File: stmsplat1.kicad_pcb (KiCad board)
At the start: 2 copper layers, 14 parts, among them CN1 C_Pack04, CN10 Conn_01x34_Male, CN7 Conn_01x20_Male, CN8 Conn_01x16_Male, CN9 Conn_01x30_Male, J1 Conn_Coaxial, J2 Conn_Coaxial, J3 Conn_Coaxial, U1 NUCLEO144-F746ZG, U2 SA630D-RF_Switch, U3 MCP6S93-X_UN, U4 ublox_chinese_PCB_module

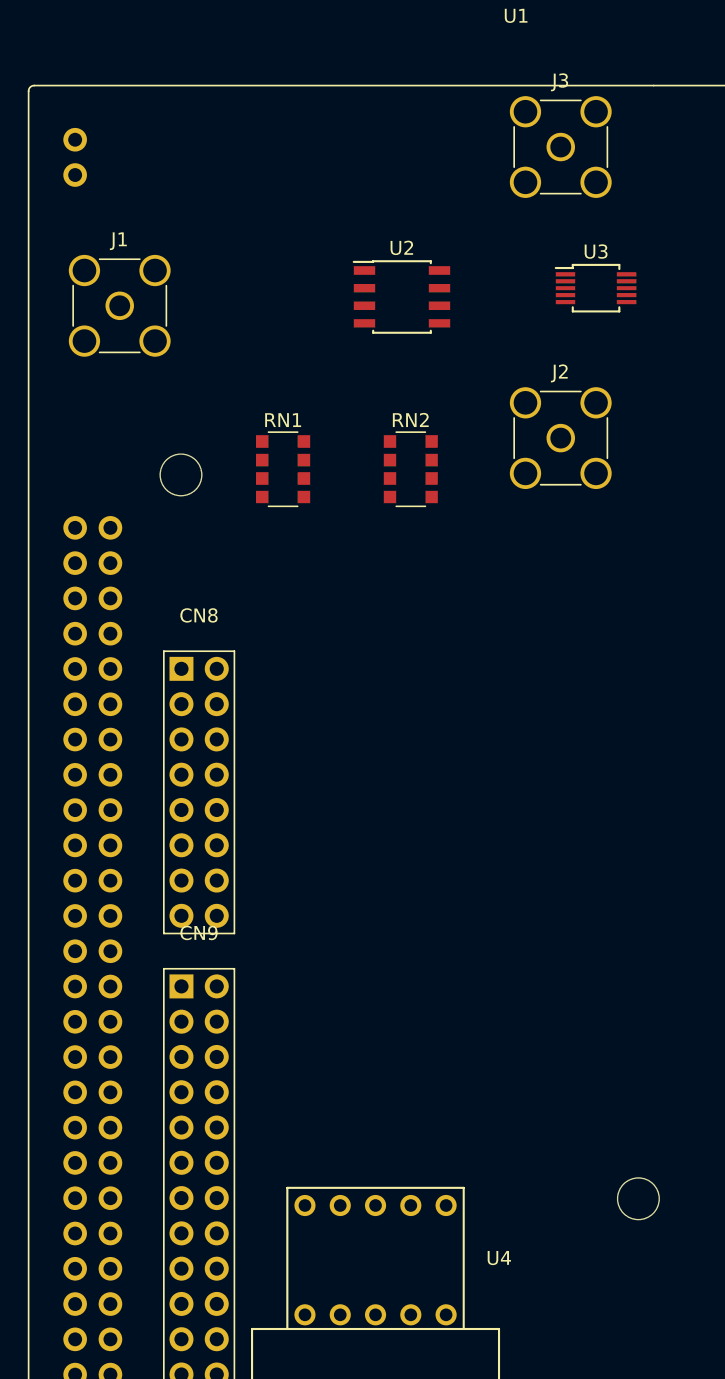
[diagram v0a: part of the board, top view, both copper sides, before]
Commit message: Added input lowpass filter
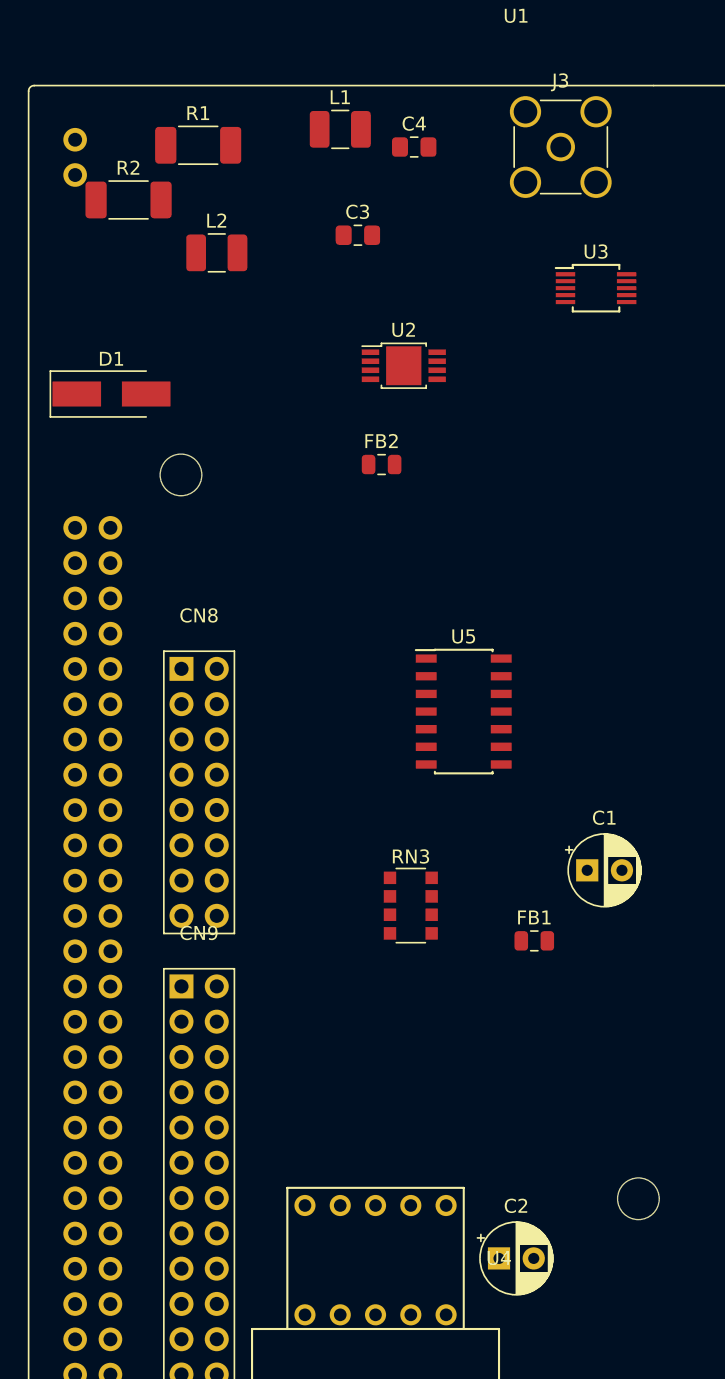
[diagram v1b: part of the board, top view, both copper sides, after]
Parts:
- removed J1, J2: Conn_Coaxial, Connector_Coaxial:SMA_Amphenol_132134-11_Vertical
- removed RN1, RN2: R_Pack04, Resistor_SMD:R_Array_Convex_4x1206
- added C1: 1uF, Capacitor_THT:CP_Radial_D5.0mm_P2.50mm, F.Cu at (95.2, 90.2)
- added C2: 1uF, Capacitor_THT:CP_Radial_D5.0mm_P2.50mm, F.Cu at (88.9, 118.1)
- added C3: 560pF, Capacitor_SMD:C_0805_2012Metric_Pad1.15x1.40mm_HandSolder, F.Cu at (78.7, 44.5)
- added C4: 240pF, Capacitor_SMD:C_0805_2012Metric_Pad1.15x1.40mm_HandSolder, F.Cu at (82.8, 38.1)
- added D1: SMAJ8.0CA Bourns 9V, Diode_SMD:D_SMA_Handsoldering, F.Cu at (61.0, 55.9)
- added FB1: Ferrite_Bead, Inductor_SMD:L_0805_2012Metric, F.Cu at (91.4, 95.2)
- added FB2: Ferrite_Bead, Inductor_SMD:L_0805_2012Metric, F.Cu at (80.4, 61.0)
- added L1: 620nH, Inductor_SMD:L_1210_3225Metric_Pad1.42x2.65mm_HandSolder, F.Cu at (77.5, 36.8)
- added L2: 1.5uH, Inductor_SMD:L_1210_3225Metric_Pad1.42x2.65mm_HandSolder, F.Cu at (68.6, 45.7)
- added R1: 100R, Resistor_SMD:R_2010_5025Metric_Pad1.52x2.65mm_HandSolder, F.Cu at (67.2, 38.0)
- added R2: 100R, Resistor_SMD:R_2010_5025Metric_Pad1.52x2.65mm_HandSolder, F.Cu at (62.2, 41.9)
- added RN3: 4K7, Resistor_SMD:R_Array_Convex_4x1206, F.Cu at (82.5, 92.7)
- added U5: Opamp_Quad_MCP6024, Package_SO:SOIC-14_3.9x8.7mm_P1.27mm, F.Cu at (86.4, 78.7)
- CN1: value C_Pack04 -> 10n
- U2: value SA630D-RF_Switch -> AD8310; footprint Package_SO:SOIC-8_3.9x4.9mm_P1.27mm -> Package_SO:MSOP-8-1EP_3x3mm_P0.65mm_EP2.54x2.8mm
- moved U2 4.95 mm to (82.0, 53.8)
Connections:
- CN10 pad 17: /GND -> GND
- CN10 pad 22: /GND -> GND
- CN10 pad 27: /GND -> GND
- CN10 pad 5: /GND -> GND
- CN7 pad 8: /GND -> GND
- CN8 pad 11: /GND -> GND
- CN9 pad 12: /GND -> GND
- CN9 pad 23: /GND -> GND
- J3 pad 1: Net-(J3-Pad1) -> Net-(D1-Pad1)
- J3 pad 2: Net-(J3-Pad2) -> /AGND
- U2 pad 2: Net-(U2-Pad2) -> /AGND
- U2 pad 5: Net-(J2-Pad1) -> /A3V3
- U2 pad 8: Net-(J3-Pad1) -> Net-(U2-Pad8)
- U3 pad 3: Net-(U3-Pad3) -> Net-(U2-Pad4)
- U3 pad 5: Net-(U3-Pad5) -> /AGND
- U4 pad 1: Net-(U4-Pad1) -> /+3V3
- U4 pad 2: Net-(U4-Pad2) -> GND

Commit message: Added more
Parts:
- added C10: 47n, Capacitor_SMD:C_1210_3225Metric_Pad1.42x2.65mm_HandSolder, F.Cu at (36.8, 92.4)
- added C11: 47n, Capacitor_SMD:C_1210_3225Metric_Pad1.42x2.65mm_HandSolder, F.Cu at (41.7, 89.2)
- added C12: 1uF, Capacitor_THT:CP_Radial_D5.0mm_P2.50mm, F.Cu at (33.9, 109.5)
- added C13: 10uF, Capacitor_THT:CP_Radial_D5.0mm_P2.50mm, F.Cu at (39.5, 109.5)
- added C14: 1uF, Capacitor_THT:CP_Radial_D5.0mm_P2.50mm, F.Cu at (28.3, 109.5)
- added C15: 100nF, Capacitor_THT:C_Disc_D7.5mm_W2.5mm_P5.00mm, F.Cu at (38.4, 30.7)
- added C16: 100uF, Capacitor_THT:CP_Radial_D5.0mm_P2.50mm, F.Cu at (46.5, 32.0)
- added C17: 100uF, Capacitor_THT:CP_Radial_D5.0mm_P2.50mm, F.Cu at (38.4, 35.0)
- added C5: 47n, Capacitor_SMD:C_1210_3225Metric_Pad1.42x2.65mm_HandSolder, F.Cu at (36.6, 64.5)
- added C6: 47n, Capacitor_SMD:C_1210_3225Metric_Pad1.42x2.65mm_HandSolder, F.Cu at (41.5, 61.3)
- added C7: 47n, Capacitor_SMD:C_1210_3225Metric_Pad1.42x2.65mm_HandSolder, F.Cu at (36.6, 61.3)
- added C8: 25pF, Capacitor_THT:C_Disc_D7.5mm_W2.5mm_P5.00mm, F.Cu at (22.9, 82.5)
- added C9: 47n, Capacitor_SMD:C_1210_3225Metric_Pad1.42x2.65mm_HandSolder, F.Cu at (36.8, 89.2)
- added D2: LED, LED_SMD:LED_PLCC-2, F.Cu at (35.1, 145.1)
- added D3: LED, LED_SMD:LED_PLCC-2, F.Cu at (35.5, 141.6)
- added D4: LED, LED_SMD:LED_PLCC-2, F.Cu at (40.7, 141.6)
- added D5: LED, LED_SMD:LED_PLCC-2, F.Cu at (39.6, 133.4)
- added D6: LED, LED_SMD:LED_PLCC-2, F.Cu at (45.0, 118.1)
- added D7: LED, LED_SMD:LED_PLCC-2, F.Cu at (34.4, 133.4)
- added J2: Conn_01x04_Male, Connector_PinHeader_2.54mm:PinHeader_1x04_P2.54mm_Vertical, F.Cu at (28.5, 36.1)
- added R3: 53R, Capacitor_SMD:C_1210_3225Metric_Pad1.42x2.65mm_HandSolder, F.Cu at (29.1, 70.6)
- added RN2: 470R, Resistor_SMD:R_Array_Convex_4x1206, F.Cu at (38.4, 123.5)
- added RN3: 470R, Resistor_SMD:R_Array_Convex_4x1206, F.Cu at (34.0, 123.5)
- added TP10: TestPoint, TestPoint:TestPoint_Loop_D1.80mm_Drill1.0mm_Beaded, F.Cu at (45.6, 68.8)
- added TP11: TestPoint, TestPoint:TestPoint_Loop_D1.80mm_Drill1.0mm_Beaded, F.Cu at (41.9, 72.5)
- added TP12: TestPoint, TestPoint:TestPoint_Loop_D1.80mm_Drill1.0mm_Beaded, F.Cu at (45.8, 61.5)
- added TP13: TestPoint, TestPoint:TestPoint_Loop_D1.80mm_Drill1.0mm_Beaded, F.Cu at (49.2, 68.8)
- added TP3: TestPoint, TestPoint:TestPoint_Loop_D1.80mm_Drill1.0mm_Beaded, F.Cu at (44.5, 65.2)
- added TP4: TestPoint, TestPoint:TestPoint_Loop_D1.80mm_Drill1.0mm_Beaded, F.Cu at (38.3, 72.0)
- added TP5: TestPoint, TestPoint:TestPoint_Loop_D1.80mm_Drill1.0mm_Beaded, F.Cu at (49.5, 61.5)
- added TP6: TestPoint, TestPoint:TestPoint_Loop_D1.80mm_Drill1.0mm_Beaded, F.Cu at (69.8, 68.6)
- added TP7: TestPoint, TestPoint:TestPoint_Loop_D1.80mm_Drill1.0mm_Beaded, F.Cu at (41.9, 68.8)
- added TP8: TestPoint, TestPoint:TestPoint_Loop_D1.80mm_Drill1.0mm_Beaded, F.Cu at (48.2, 65.2)
- added TP9: TestPoint, TestPoint:TestPoint_Loop_D1.80mm_Drill1.0mm_Beaded, F.Cu at (45.6, 72.5)
- added U10: MPL315A2, Package_LGA:LGA-8_3x5mm_P1.25mm, F.Cu at (44.5, 47.0)
- added U3: HMC544A-RF_Switch, Package_TO_SOT_SMD:SOT-23-6_Handsoldering, F.Cu at (101.6, 61.0)
- added U7: ADG729, Package_SO:TSSOP-16_4.4x5mm_P0.65mm, F.Cu at (97.8, 102.9)
- added U8: 74HC04, Package_SO:SOIC-14_3.9x8.7mm_P1.27mm, F.Cu at (30.4, 64.4)
- added U9: HMC544A-RF_Switch, Package_TO_SOT_SMD:SOT-23-6_Handsoldering, F.Cu at (34.0, 70.9)
- C4: renamed from C1; value 1uF -> 10uF
- renumbered C2 to C1, C3 to C2, C4 to C3, CN8 to CN1, CN9 to CN2, CN7 to CN3, CN10 to CN4, CN1 to CN5, J3 to J1, R2 to R1, R1 to R2, RN3 to RN1, U4 to U2, U5 to U4, U2 to U5, U3 to U6
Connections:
- net /AGND renamed AGND
- net Net-(U3-Pad4) renamed /HALF3V3
- C3 pad 1: Net-(C4-Pad1) -> Net-(C11-Pad1)
- D1 pad 1: Net-(D1-Pad1) -> Net-(C5-Pad1)
- J1 pad 1: Net-(D1-Pad1) -> Net-(C5-Pad2)
- L1 pad 2: Net-(D1-Pad1) -> Net-(C10-Pad2)
- L2 pad 1: Net-(C4-Pad1) -> Net-(C11-Pad1)
- R1 pad 1: Net-(D1-Pad1) -> Net-(C10-Pad2)
- R2 pad 2: Net-(D1-Pad1) -> Net-(C10-Pad2)
- RN1 pad 2: Net-(C4-Pad1) -> Net-(C11-Pad1)
- U5 pad 4: Net-(U2-Pad4) (its old number) -> /LOGOUT
- U6 pad 1: Net-(U3-Pad1) -> /AMPOUT
- U6 pad 10: Net-(U3-Pad10) -> /A3V3
- U6 pad 2: Net-(U3-Pad2) -> Net-(C11-Pad1)
- U6 pad 3: Net-(U2-Pad4) (its old number) -> Net-(U6-Pad3)

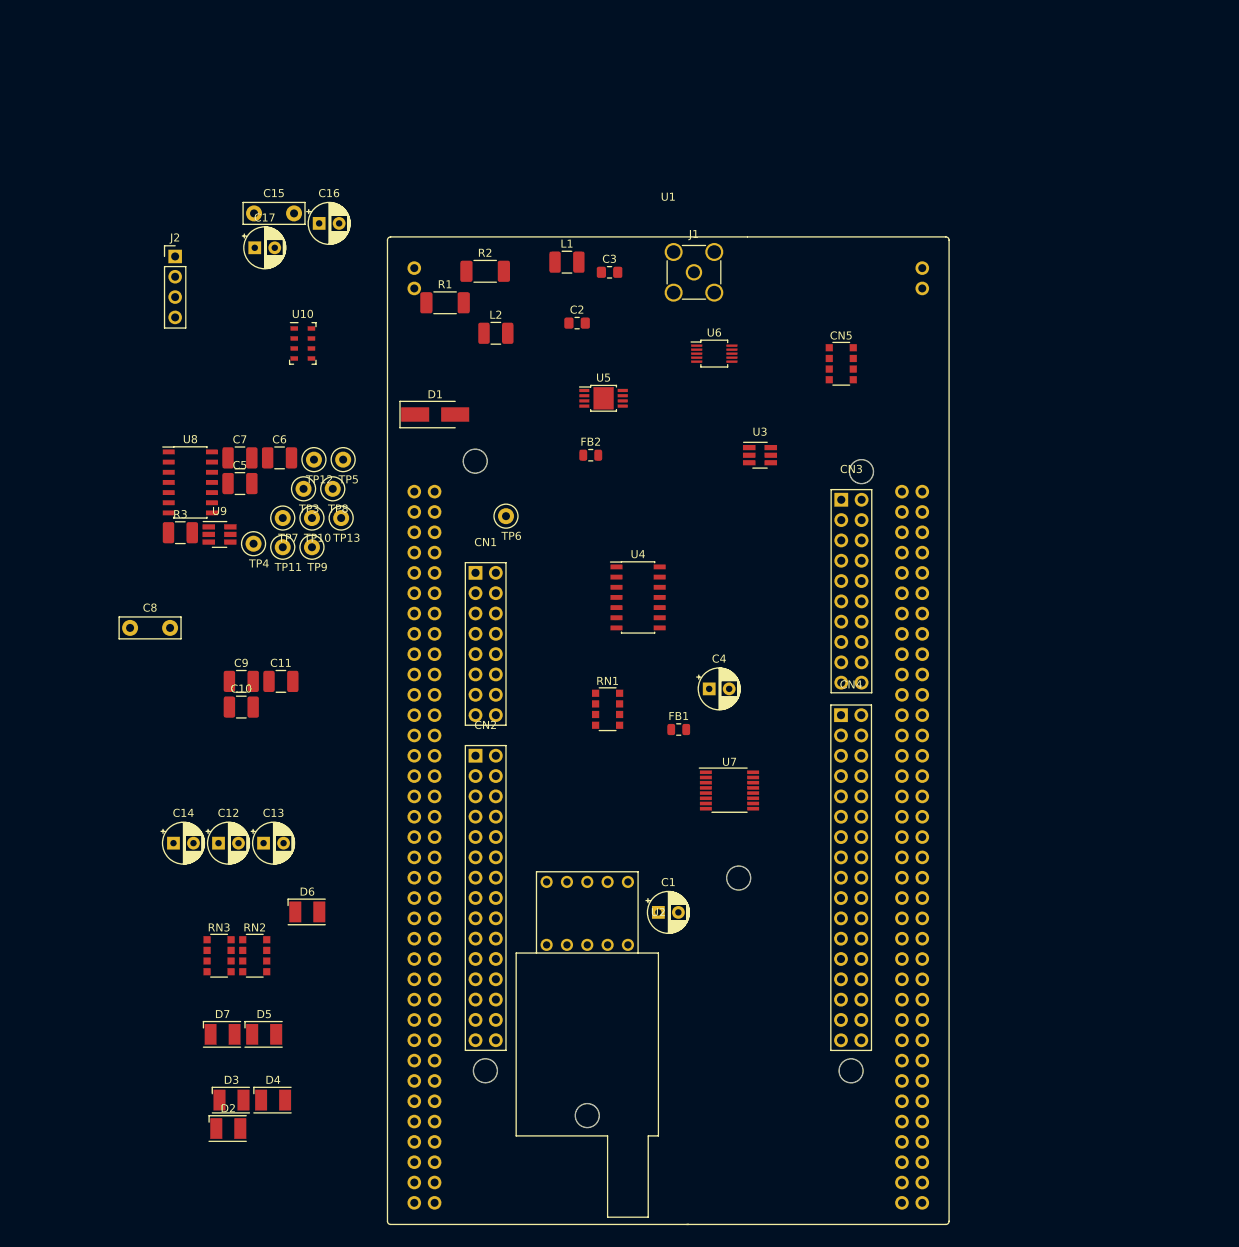
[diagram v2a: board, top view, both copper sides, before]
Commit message: Zigbee added
Trial placement 1
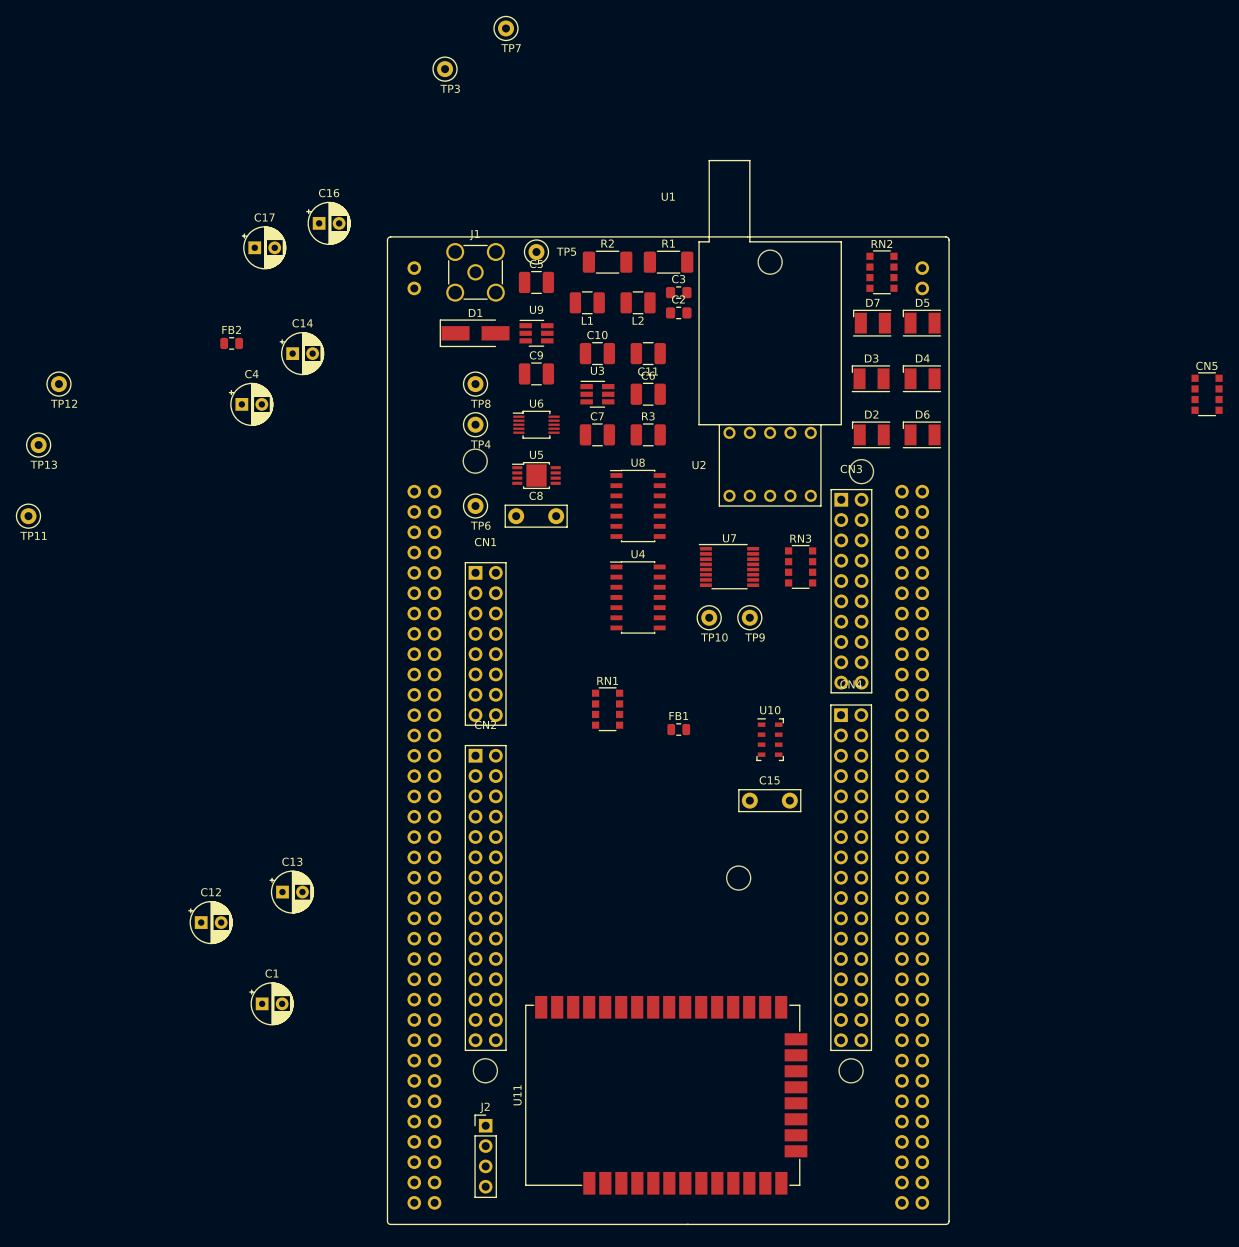
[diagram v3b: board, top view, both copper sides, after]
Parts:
- added U11: XBee_SMT, RF_Module:Digi_XBee_SMT, F.Cu at (90.2, 141.0)
- moved D4 121.3 mm to (121.9, 51.4)
- moved D5 121.1 mm to (121.9, 44.5)
- moved D3 120.5 mm to (115.5, 51.4)
- moved D7 120.5 mm to (115.7, 44.5)
- moved D2 118.3 mm to (115.6, 58.4)
- moved RN2 115.9 mm to (116.8, 38.1)
- moved J2 115.4 mm to (67.3, 144.8)
- moved D6 97.3 mm to (121.9, 58.4)
- moved C15 96.1 mm to (100.3, 104.1)
- moved RN3 87.4 mm to (106.7, 74.9)
- moved U10 76.6 mm to (102.9, 96.5)
- moved C4 68.4 mm to (36.8, 54.6)
- moved TP7 67.3 mm to (69.8, 7.62)
- moved C14 63.0 mm to (43.2, 48.3)
- moved C10 62.7 mm to (81.3, 48.3)
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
